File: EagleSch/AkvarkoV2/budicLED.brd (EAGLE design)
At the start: 114.3 x 160 mm, 89 parts, among them IC1 7805T, IC2 4051N, IC3 LF33CV, IC4 ESP01, J1 TRANSFLASH-LOCK, Q1 BD243C, Q2 BD243C, Q3 BD243C, Q4 BD243C, Q5 BC546A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

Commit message: - upraveny hodnoty odporu u zesilovace napeti z bocniku - pridana dioda do napajeciho vstupu ARDUINO
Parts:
- added D5: (no value), diode:MELF-MLL41
- R33: value 10k -> 12k
- R35: value 10k -> 2k4
- moved R21 11.7 mm to (105.4, 24.1), turned to 90 degrees
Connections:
- new net N$48: D5.C, U1.VIN
- net +12V: now also D5.A; no longer U1.VIN
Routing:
- net +12V: track 377.7 -> 355.0 mm
- net N$48: track 0.00 -> 17.5 mm
- net N$23: track 87.6 -> 89.6 mm
- net N$10: track 96.0 -> 94.7 mm
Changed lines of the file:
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@@
 <grid distance="0.05" unitdist="inch" unit="inch" style="lines" multiple="1" display="no" altdistance="0.0125" altunitdist="inch" altunit="inch"/>
 <layers>
-<layer number="1" name="Top" color="4" fill="1" visible="yes" active="yes"/>
+<layer number="1" name="Top" color="4" fill="1" visible="no" active="yes"/>
 <layer number="2" name="Route2" color="1" fill="3" visible="no" active="no"/>
 <layer number="3" name="Route3" color="4" fill="3" visible="no" active="no"/>
@@
 <layer number="39" name="tKeepout" color="4" fill="11" visible="yes" active="yes"/>
 <layer number="40" name="bKeepout" color="1" fill="11" visible="yes" active="yes"/>
-<layer number="41" name="tRestrict" color="4" fill="10" visible="yes" active="yes"/>
-<layer number="42" name="bRestrict" color="1" fill="10" visible="yes" active="yes"/>
-<layer number="43" name="vRestrict" color="2" fill="10" visible="yes" active="yes"/>
+<layer number="41" name="tRestrict" color="4" fill="10" visible="no" active="yes"/>
+<layer number="42" name="bRestrict" color="1" fill="10" visible="no" active="yes"/>
+<layer number="43" name="vRestrict" color="2" fill="10" visible="no" active="yes"/>
 <layer number="44" name="Drills" color="7" fill="1" visible="no" active="yes"/>
 <layer number="45" name="Holes" color="7" fill="1" visible="no" active="yes"/>
 <layer number="46" name="Milling" color="3" fill="1" visible="no" active="yes"/>
 <layer number="47" name="Measures" color="7" fill="1" visible="no" active="yes"/>
-<layer number="48" name="Document" color="7" fill="1" visible="yes" active="yes"/>
-<layer number="49" name="Reference" color="7" fill="1" visible="yes" active="yes"/>
+<layer number="48" name="Document" color="7" fill="1" visible="no" active="yes"/>
+<layer number="49" name="Reference" color="7" fill="1" visible="no" active="yes"/>
 <layer number="50" name="dxf" color="7" fill="1" visible="no" active="yes"/>
-<layer number="51" name="tDocu" color="7" fill="1" visible="yes" active="yes"/>
-<layer number="52" name="bDocu" color="7" fill="1" visible="yes" active="yes"/>
+<layer number="51" name="tDocu" color="7" fill="1" visible="no" active="yes"/>
+<layer number="52" name="bDocu" color="7" fill="1" visible="no" active="yes"/>
 <layer number="53" name="tGND_GNDA" color="7" fill="9" visible="no" active="no"/>
 <layer number="54" name="bGND_GNDA" color="1" fill="9" visible="no" active="no"/>
@@
 <layer number="127" name="_tValues" color="7" fill="1" visible="no" active="yes"/>
 <layer number="128" name="_bValues" color="7" fill="1" visible="no" active="yes"/>
-<layer number="129" name="Mask" color="7" fill="1" visible="yes" active="yes"/>
+<layer number="129" name="Mask" color="7" fill="1" visible="no" active="yes"/>
 <layer number="131" name="tAdjust" color="7" fill="1" visible="no" active="yes"/>
 <layer number="132" name="bAdjust" color="7" fill="1" visible="no" active="yes"/>
@@
 <layer number="223" name="223bmp" color="24" fill="1" visible="no" active="no"/>
 <layer number="224" name="224bmp" color="25" fill="1" visible="no" active="no"/>
-<layer number="225" name="225bmp" color="7" fill="1" visible="yes" active="yes"/>
-<layer number="226" name="226bmp" color="7" fill="1" visible="yes" active="yes"/>
-<layer number="227" name="227bmp" color="7" fill="1" visible="yes" active="yes"/>
-<layer number="228" name="228bmp" color="7" fill="1" visible="yes" active="yes"/>
-<layer number="229" name="229bmp" color="7" fill="1" visible="yes" active="yes"/>
-<layer number="230" name="230bmp" color="7" fill="1" visible="yes" active="yes"/>
+<layer number="225" name="225bmp" color="7" fill="1" visible="no" active="yes"/>
+<layer number="226" name="226bmp" color="7" fill="1" visible="no" active="yes"/>
+<layer number="227" name="227bmp" color="7" fill="1" visible="no" active="yes"/>
+<layer number="228" name="228bmp" color="7" fill="1" visible="no" active="yes"/>
+<layer number="229" name="229bmp" color="7" fill="1" visible="no" active="yes"/>
+<layer number="230" name="230bmp" color="7" fill="1" visible="no" active="yes"/>
 <layer number="231" name="Eagle3D_PG1" color="7" fill="1" visible="no" active="no"/>
 <layer number="232" name="Eagle3D_PG2" color="7" fill="1" visible="no" active="no"/>
@@
 <layer number="251" name="SMDround" color="7" fill="1" visible="no" active="no"/>
 <layer number="254" name="cooling" color="7" fill="1" visible="no" active="yes"/>
-<layer number="255" name="routoute" color="7" fill="1" visible="yes" active="yes"/>
+<layer number="255" name="routoute" color="7" fill="1" visible="no" active="yes"/>
 </layers>
 <board>
@@
 <element name="C5" library="rcl" package="C1206K" value="330n" x="93.98" y="20.32" rot="MR180"/>
 <element name="C6" library="rcl" package="C1206K" value="100n" x="96.52" y="24.13" rot="MR0"/>
-<element name="R21" library="rcl" package="0207/12" value="4k7" x="102.87" y="12.7" rot="R270"/>
+<element name="R21" library="rcl" package="0207/12" value="4k7" x="105.41" y="24.13" rot="R90"/>
 <element name="C7" library="resistor" package="E5-10,5" value="10u" x="83.82" y="48.26" rot="R180"/>
 <element name="U$1" library="holes" package="3,2" value="" x="5.08" y="154.94"/>
@@
 <element name="C13" library="rcl" package="C1206K" value="100n" x="77.47" y="139.3825" rot="MR270"/>
 <element name="Q5" library="transistor-npn" package="TO92-EBC" value="BC546A" x="29.21" y="105.41" rot="R180"/>
-<element name="R33" library="rcl" package="0207/12" value="10k" x="31.75" y="115.57" rot="R90"/>
+<element name="R33" library="rcl" package="0207/12" value="12k" x="31.75" y="115.57" rot="R90"/>
 <element name="R34" library="rcl" package="0207/12" value="10k" x="29.21" y="115.57" rot="R270"/>
-<element name="R35" library="rcl" package="0207/12" value="10k" x="26.67" y="115.57" rot="R90"/>
+<element name="R35" library="rcl" package="0207/12" value="2k4" x="26.67" y="115.57" rot="R90"/>
 <element name="C14" library="rcl" package="C1206K" value="100n" x="30.48" y="104.14" rot="MR0"/>
 <element name="LED2" library="led" package="LED3MM" value="2.2V 25mA" x="77.47" y="90.17" rot="R270"/>
@@
 <element name="R40" library="rcl" package="0207/12" value="0R0" x="69.215" y="140.97" rot="R180"/>
 <element name="R41" library="rcl" package="0207/12" value="0R0" x="105.41" y="114.3" rot="R180"/>
+<element name="D5" library="diode" package="MELF-MLL41" value="" x="20.32" y="116.84" rot="MR0"/>
 </elements>
 <signals>
@@
 <contactref element="IC3" pad="1"/>
 <contactref element="C9" pad="1"/>
-<contactref element="U1" pad="VIN"/>
 <contactref element="X2" pad="2"/>
 <contactref element="X2" pad="4"/>
@@
 <wire x1="94.615" y1="75.16" x2="91.67" y2="75.16" width="1.27" layer="16"/>
 <wire x1="91.67" y1="75.16" x2="91.44" y2="74.93" width="1.27" layer="16"/>
-<wire x1="39.37" y1="114.3" x2="38.1" y2="114.3" width="1.778" layer="16"/>
-<wire x1="38.1" y1="114.3" x2="35.56" y2="116.84" width="1.778" layer="16"/>
-<wire x1="35.56" y1="116.84" x2="15.24" y2="116.84" width="1.778" layer="16"/>
+<contactref element="D5" pad="A"/>
+<wire x1="15.24" y1="116.84" x2="17.695" y2="116.84" width="1.6764" layer="16"/>
 </signal>
 <signal name="N$21">
@@
 <wire x1="97.79" y1="17.78" x2="97.79" y2="21.59" width="1.016" layer="16"/>
 <contactref element="R22" pad="1"/>
-<wire x1="97.79" y1="17.78" x2="101.6" y2="17.78" width="1.016" layer="16"/>
-<wire x1="101.6" y1="17.78" x2="102.87" y2="19.05" width="1.016" layer="16"/>
+<wire x1="97.79" y1="17.78" x2="105.41" y2="17.78" width="1.016" layer="16"/>
 <wire x1="98.02" y1="24.13" x2="101.6" y2="24.13" width="1.016" layer="16"/>
 <wire x1="101.6" y1="24.13" x2="102.87" y2="25.4" width="1.016" layer="16"/>
@@
 <contactref element="R21" pad="2"/>
 <contactref element="R24" pad="1"/>
-<wire x1="95.25" y1="43.18" x2="86.36" y2="52.07" width="1.016" layer="16"/>
-<wire x1="92.75" y1="8.89" x2="92.75" y2="8.85" width="1.016" layer="16"/>
-<wire x1="92.75" y1="8.85" x2="95.25" y2="6.35" width="1.016" layer="16"/>
-<wire x1="95.25" y1="6.35" x2="102.87" y2="6.35" width="1.016" layer="16"/>
-<wire x1="102.87" y1="6.35" x2="102.87" y2="13.97" width="1.016" layer="16"/>
-<wire x1="102.87" y1="13.97" x2="105.41" y2="16.51" width="1.016" layer="16"/>
-<wire x1="105.41" y1="16.51" x2="105.41" y2="39.37" width="1.016" layer="16"/>
-<wire x1="105.41" y1="39.37" x2="101.6" y2="43.18" width="1.016" layer="16"/>
-<wire x1="101.6" y1="43.18" x2="95.25" y2="43.18" width="1.016" layer="16"/>
-<wire x1="86.36" y1="52.07" x2="86.36" y2="74.93" width="1.016" layer="16"/>
-<wire x1="83.82" y1="77.47" x2="86.36" y2="74.93" width="1.016" layer="16"/>
+<wire x1="92.75" y1="8.89" x2="92.75" y2="7.58" width="1.016" layer="16"/>
+<wire x1="92.75" y1="7.58" x2="95.25" y2="5.08" width="1.016" layer="16"/>
+<wire x1="95.25" y1="5.08" x2="99.06" y2="5.08" width="1.016" layer="16"/>
+<wire x1="99.06" y1="5.08" x2="101.6" y2="7.62" width="1.016" layer="16"/>
+<wire x1="101.6" y1="7.62" x2="101.6" y2="10.16" width="1.016" layer="16"/>
+<wire x1="101.6" y1="10.16" x2="107.95" y2="16.51" width="1.016" layer="16"/>
+<wire x1="107.95" y1="16.51" x2="107.95" y2="27.94" width="1.016" layer="16"/>
+<wire x1="107.95" y1="27.94" x2="105.41" y2="30.48" width="1.016" layer="16"/>
+<wire x1="105.41" y1="30.48" x2="105.41" y2="38.1" width="1.016" layer="16"/>
+<wire x1="105.41" y1="38.1" x2="86.36" y2="57.15" width="1.016" layer="16"/>
+<wire x1="86.36" y1="57.15" x2="86.36" y2="74.93" width="1.016" layer="16"/>
+<wire x1="86.36" y1="74.93" x2="83.82" y2="77.47" width="1.016" layer="16"/>
 </signal>
 <signal name="N$16">
@@
 <wire x1="77.3825" y1="140.97" x2="77.47" y2="140.8825" width="1.27" layer="16"/>
 </signal>
+<signal name="N$48">
+<contactref element="D5" pad="C"/>
+<contactref element="U1" pad="VIN"/>
+<wire x1="22.945" y1="116.84" x2="34.29" y2="116.84" width="1.6764" layer="16"/>
+<wire x1="34.29" y1="116.84" x2="36.83" y2="114.3" width="1.6764" layer="16"/>
+<wire x1="36.83" y1="114.3" x2="39.37" y2="114.3" width="1.6764" layer="16"/>
+</signal>
 </signals>

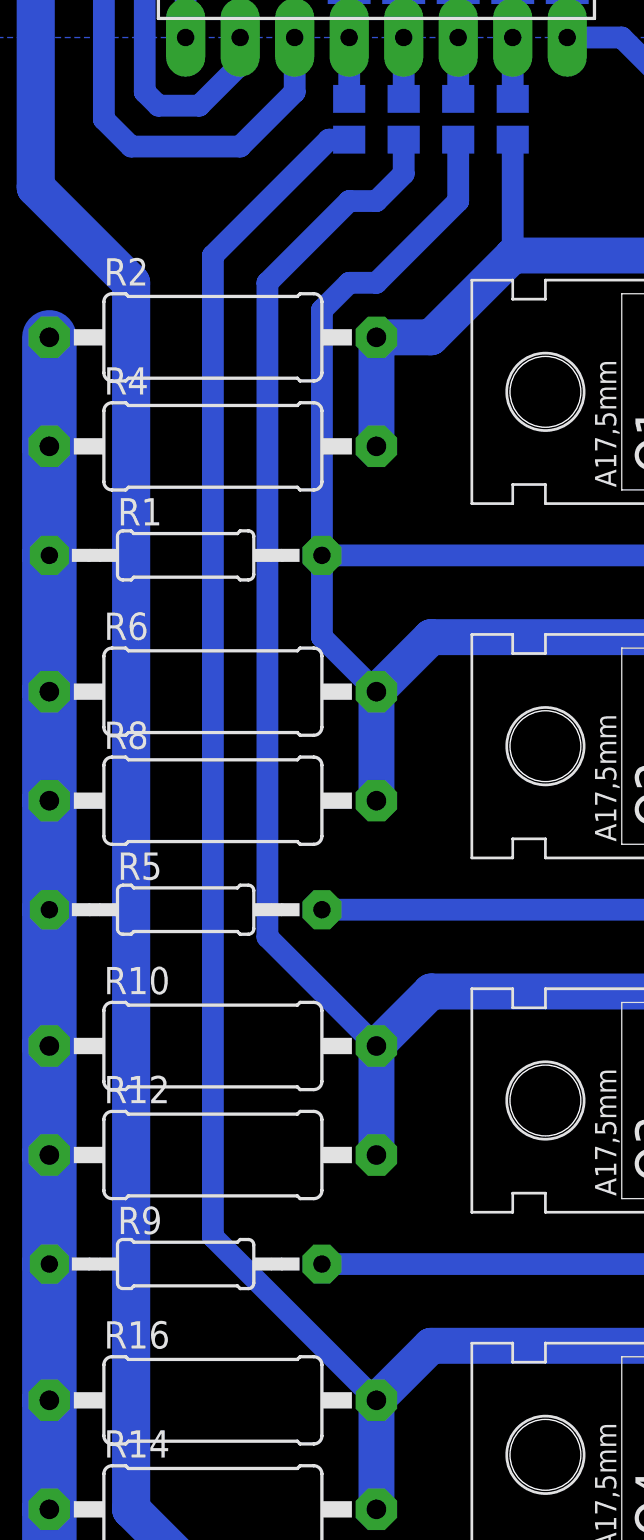
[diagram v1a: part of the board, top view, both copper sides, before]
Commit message: DPS: - opravena chybna cesta u rezistoru R1
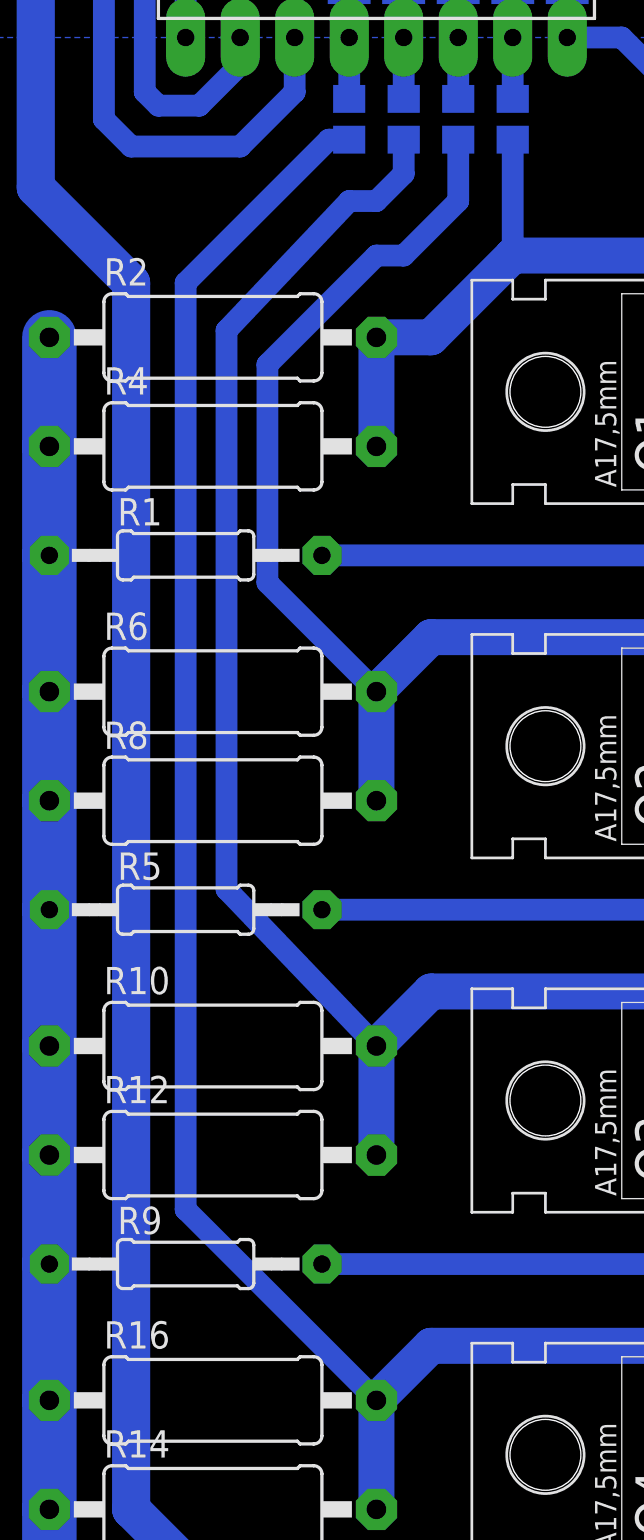
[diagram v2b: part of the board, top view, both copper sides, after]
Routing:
- net SENS3: track 62.7 -> 64.8 mm
- net SENS2: track 80.3 -> 81.7 mm
- net SENS1: track 97.7 -> 98.7 mm
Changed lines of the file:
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@@
 <wire x1="19.05" y1="30.48" x2="19.05" y2="25.4" width="1.6764" layer="16"/>
 <wire x1="17.78" y1="89.22" x2="16.83" y2="89.22" width="1.016" layer="16"/>
-<wire x1="16.83" y1="89.22" x2="11.43" y2="83.82" width="1.016" layer="16"/>
-<wire x1="11.43" y1="83.82" x2="11.43" y2="38.1" width="1.016" layer="16"/>
-<wire x1="11.43" y1="38.1" x2="19.05" y2="30.48" width="1.016" layer="16"/>
+<wire x1="16.83" y1="89.22" x2="10.16" y2="82.55" width="1.016" layer="16"/>
+<wire x1="10.16" y1="82.55" x2="10.16" y2="39.37" width="1.016" layer="16"/>
+<wire x1="10.16" y1="39.37" x2="19.05" y2="30.48" width="1.016" layer="16"/>
 <wire x1="19.05" y1="30.48" x2="21.59" y2="33.02" width="1.6764" layer="16"/>
 <wire x1="21.59" y1="33.02" x2="41.91" y2="33.02" width="1.6764" layer="16"/>
@@
 <wire x1="20.32" y1="87.63" x2="19.05" y2="86.36" width="1.016" layer="16"/>
 <wire x1="19.05" y1="86.36" x2="17.78" y2="86.36" width="1.016" layer="16"/>
-<wire x1="17.78" y1="86.36" x2="13.97" y2="82.55" width="1.016" layer="16"/>
-<wire x1="13.97" y1="82.55" x2="13.97" y2="52.07" width="1.016" layer="16"/>
-<wire x1="13.97" y1="52.07" x2="19.05" y2="46.99" width="1.016" layer="16"/>
+<wire x1="17.78" y1="86.36" x2="12.065" y2="80.3275" width="1.016" layer="16"/>
+<wire x1="12.065" y1="80.3275" x2="12.065" y2="54.2925" width="1.016" layer="16"/>
+<wire x1="12.065" y1="54.2925" x2="19.05" y2="46.99" width="1.016" layer="16"/>
 <wire x1="19.05" y1="46.99" x2="21.59" y2="49.53" width="1.6764" layer="16"/>
 <wire x1="21.59" y1="49.53" x2="41.91" y2="49.53" width="1.6764" layer="16"/>
@@
 <wire x1="19.05" y1="63.5" x2="19.05" y2="58.42" width="1.6764" layer="16"/>
 <wire x1="22.86" y1="89.22" x2="22.86" y2="86.36" width="1.016" layer="16"/>
-<wire x1="22.86" y1="86.36" x2="19.05" y2="82.55" width="1.016" layer="16"/>
-<wire x1="19.05" y1="82.55" x2="17.78" y2="82.55" width="1.016" layer="16"/>
-<wire x1="17.78" y1="82.55" x2="16.51" y2="81.28" width="1.016" layer="16"/>
-<wire x1="16.51" y1="81.28" x2="16.51" y2="66.04" width="1.016" layer="16"/>
-<wire x1="16.51" y1="66.04" x2="19.05" y2="63.5" width="1.016" layer="16"/>
+<wire x1="22.86" y1="86.36" x2="20.32" y2="83.82" width="1.016" layer="16"/>
+<wire x1="20.32" y1="83.82" x2="19.05" y2="83.82" width="1.016" layer="16"/>
 <wire x1="44.45" y1="63.5" x2="41.91" y2="66.04" width="1.6764" layer="16"/>
 <wire x1="41.91" y1="66.04" x2="21.59" y2="66.04" width="1.6764" layer="16"/>
 <wire x1="21.59" y1="66.04" x2="19.05" y2="63.5" width="1.6764" layer="16"/>
+<wire x1="19.05" y1="63.5" x2="13.97" y2="68.58" width="1.016" layer="16"/>
+<wire x1="13.97" y1="68.58" x2="13.97" y2="78.74" width="1.016" layer="16"/>
+<wire x1="13.97" y1="78.74" x2="19.05" y2="83.82" width="1.016" layer="16"/>
 </signal>
 <signal name="SENS4">
